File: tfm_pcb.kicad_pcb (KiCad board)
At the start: 2 copper layers, 73 x 55 mm, 70 parts, among them J1 Conn_01x02_MountingPin, J12 Conn_01x01_Pin, J13 Conn_01x01_Pin, J15 Conn_01x01_Socket, J16 Conn_01x01_Socket, J17 Conn_01x01_Socket, J18 Conn_01x01_Socket, J19 Conn_01x01_Socket, J2 USB_B_Micro, J20 Conn_01x01_Socket, J21 Conn_01x01_Socket, J22 Conn_01x01_Socket, J23 Conn_01x01_Socket, J24 Conn_01x01_Socket, J3 Mounting Pin, J5 Conn_01x01_Pin, J6 Conn_01x01_Pin, U1 ESP32-S3-WROOM-2, U2 MCP73871-2CC, U3 ADS1292IPBS, U4 LSM6DS3, U5 USBLC6-2SC6, U6 XC6220B331MR, U7 USBLC6-2SC6

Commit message: Separar DVDD de la ferrita, filtro amortiguado en AVDD y conector THT de electrodos
- DVDD del ADS1292 (y C6/C7) a +3.3V sin ferrita.
- Rama analógica: FB1 + R15 (2.2 ohm) + C26 (10 uF) antes de AVDD; filtro
  colocado junto al AFE manteniendo el puente en B.Cu bajo el ADS1292.
- C12 (VREFP) sincronizado a 10 uF en la PCB.
- Esquemático: pastillas de electrodos sustituidas por conector THT 1x10.
- Documentación movida a docs_local/ (ignorada por git).

Co-Authored-By: Claude Opus 5.5 <noreply@anthropic.com>
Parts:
- added C26: 10u, Capacitor_SMD:C_0805_2012Metric, F.Cu at (168.4, 78.5)
- added R15: 2.2, Resistor_SMD:R_0603_1608Metric, F.Cu at (165.8, 77.5)
- C12: value 1u -> 10u
- FB1: value (none) -> FerriteBead
- moved FB1 25.1 mm to (162.6, 77.5)
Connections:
- C6 pad 2: +3.3VA -> +3.3V
- C7 pad 2: +3.3VA -> +3.3V
- FB1 pad 2: +3.3VA -> Net-(FB1-Pad2)
- U3 pad 23: +3.3VA -> +3.3V
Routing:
- net +3.3V: track 87.0 -> 126.3 mm, vias 2 -> 4
- net +3.3VA: track 49.6 -> 19.7 mm, vias 2 -> 0
- net Net-(FB1-Pad2): track 0.00 -> 1.59 mm

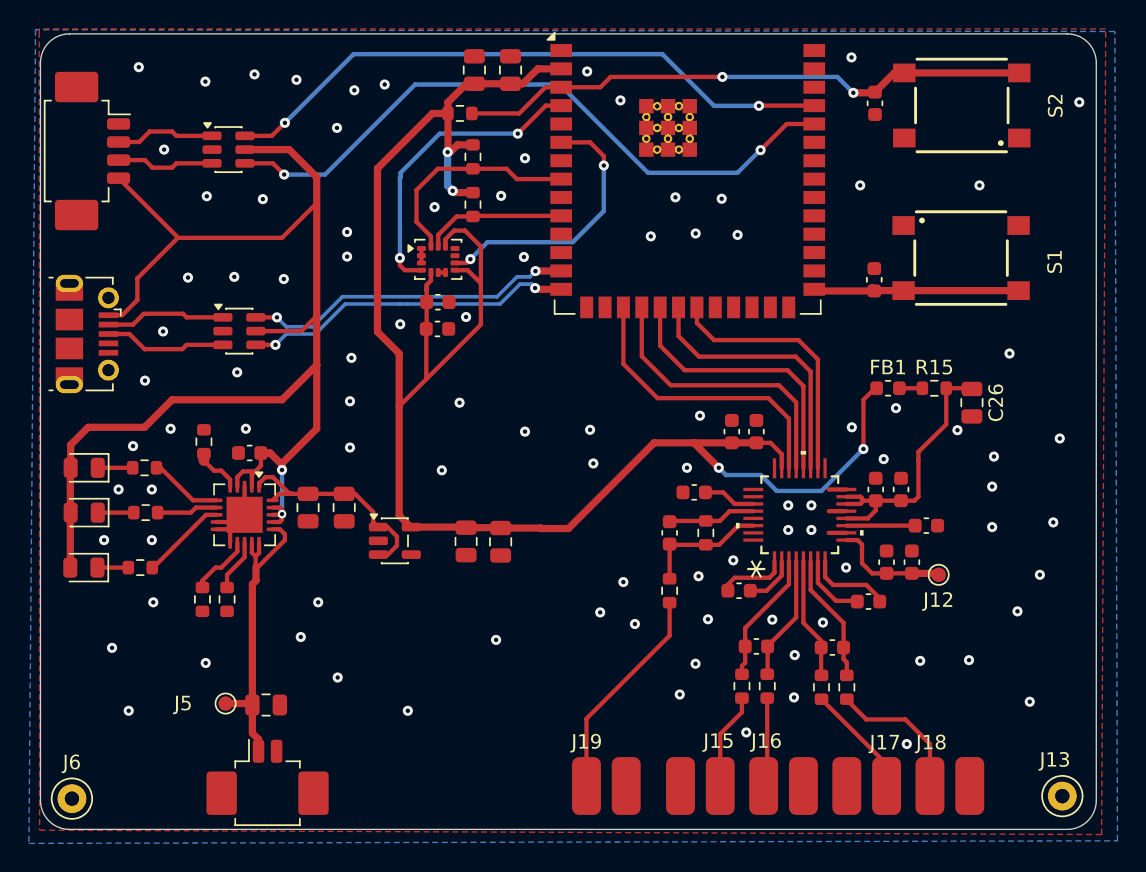
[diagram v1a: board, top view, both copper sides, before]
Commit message: Conector J4 THT reordenado, selector de malla JP1 y net SHIELD
- J4 (tira 1x10): 1 RLD, 2-3 malla, 4 IN1N, 5 IN1P, 6-7 malla, 8 IN2N,
  9 IN2P, 10 malla; etiquetas EL1N/EL1P/EL2N/EL2P en lugar del abanico.
- Net SHIELD con las cinco mallas; JP1 (tira 3 pines): 1-2 INRLD (T2),
  2-3 GND (T1). Serigrafía de función en J4 y JP1.
- Ajustes de layout del autor: filtro FB1/R15/C26 junto a C9, C26 en
  0603, SHIELD por B.Cu en el borde, rutado de EL2P.

Co-Authored-By: Claude Opus 5.5 <noreply@anthropic.com>
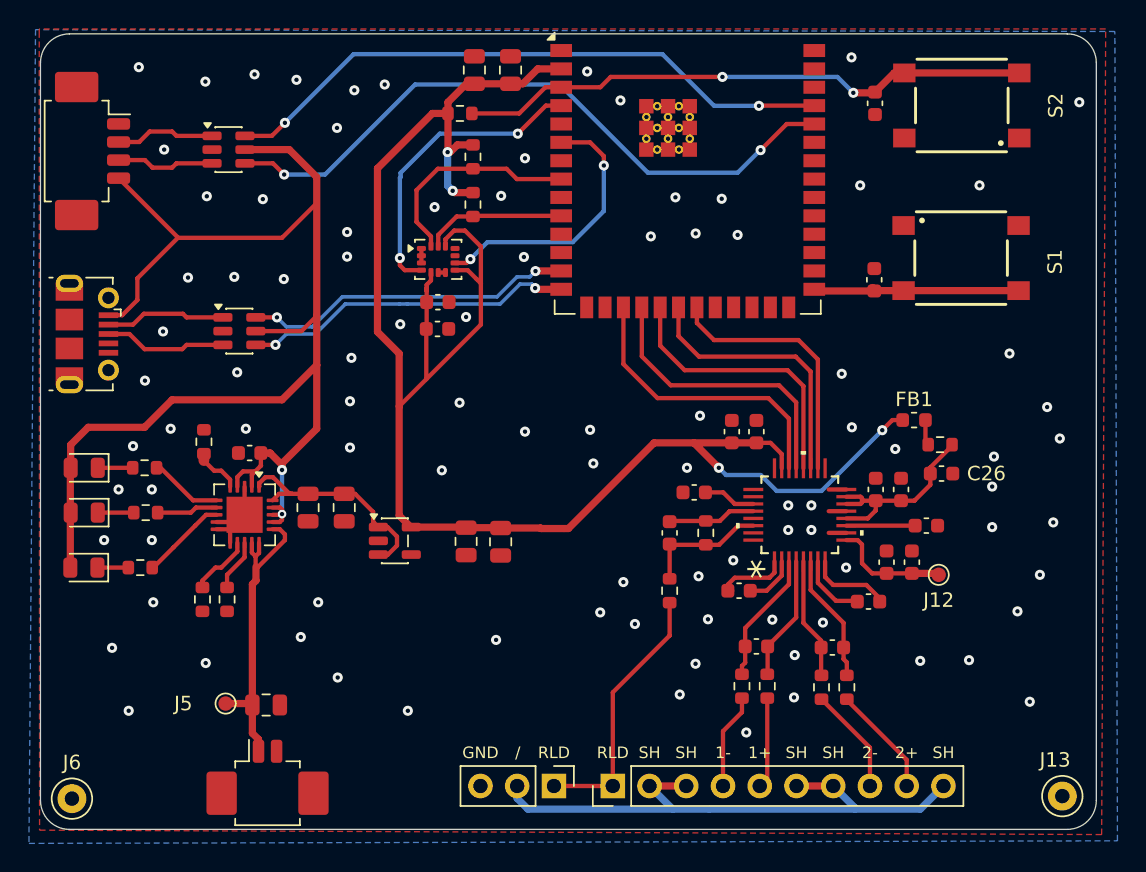
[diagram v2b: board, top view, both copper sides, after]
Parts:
- removed J15, J16, J17, J18, J19, J20, J21, J22, J23, J24: Conn_01x01_Socket, Connector_Wire:SolderWirePad_1x01_SMD_2x4mm
- added J4: Conn_01x10_Pin, Connector_PinHeader_2.54mm:PinHeader_1x10_P2.54mm_Vertical, F.Cu at (143.6, 105.0)
- added JP1: SHIELD_SEL, Connector_PinHeader_2.54mm:PinHeader_1x03_P2.54mm_Vertical, F.Cu at (139.5, 105.0)
- C26: footprint Capacitor_SMD:C_0805_2012Metric -> Capacitor_SMD:C_0603_1608Metric
- moved C26 5.33 mm to (166.3, 83.4), turned to 0 degrees
- moved R15 3.92 mm to (166.2, 81.4)
- moved FB1 2.84 mm to (164.4, 79.7)
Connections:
- R10 pad 1: Net-(J18-Pin_1) -> /EL2P
- R7 pad 1: Net-(J15-Pin_1) -> /EL1N
- R8 pad 1: Net-(J16-Pin_1) -> /EL1P
- R9 pad 1: Net-(J17-Pin_1) -> /EL2N
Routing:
- net /SHIELD: track 0.00 -> 40.9 mm
- net Net-(J18-Pin_1): track 9.96 -> 0.00 mm
- net Net-(J17-Pin_1): track 7.86 -> 0.00 mm
- net /EL2P: track 0.00 -> 7.71 mm
- net /EL2N: track 0.00 -> 7.39 mm
- net Net-(J15-Pin_1): track 6.70 -> 0.00 mm
- net /EL1N: track 0.00 -> 6.62 mm
- net /EL1P: track 0.00 -> 6.30 mm
- net Net-(J16-Pin_1): track 6.18 -> 0.00 mm
- net +3.3VA: track 19.7 -> 14.1 mm
- net /INRLD: track 15.1 -> 18.4 mm
- net +3.3V: track 126.3 -> 125.2 mm
- net GND: vias 95 -> 94
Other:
- board text added: "/"
- board text added: "1+"
- board text added: "1-"
- board text added: "2+"
- board text added: "2-"
- board text added: "GND"
- board text added: "RLD"
- board text added: "SH"

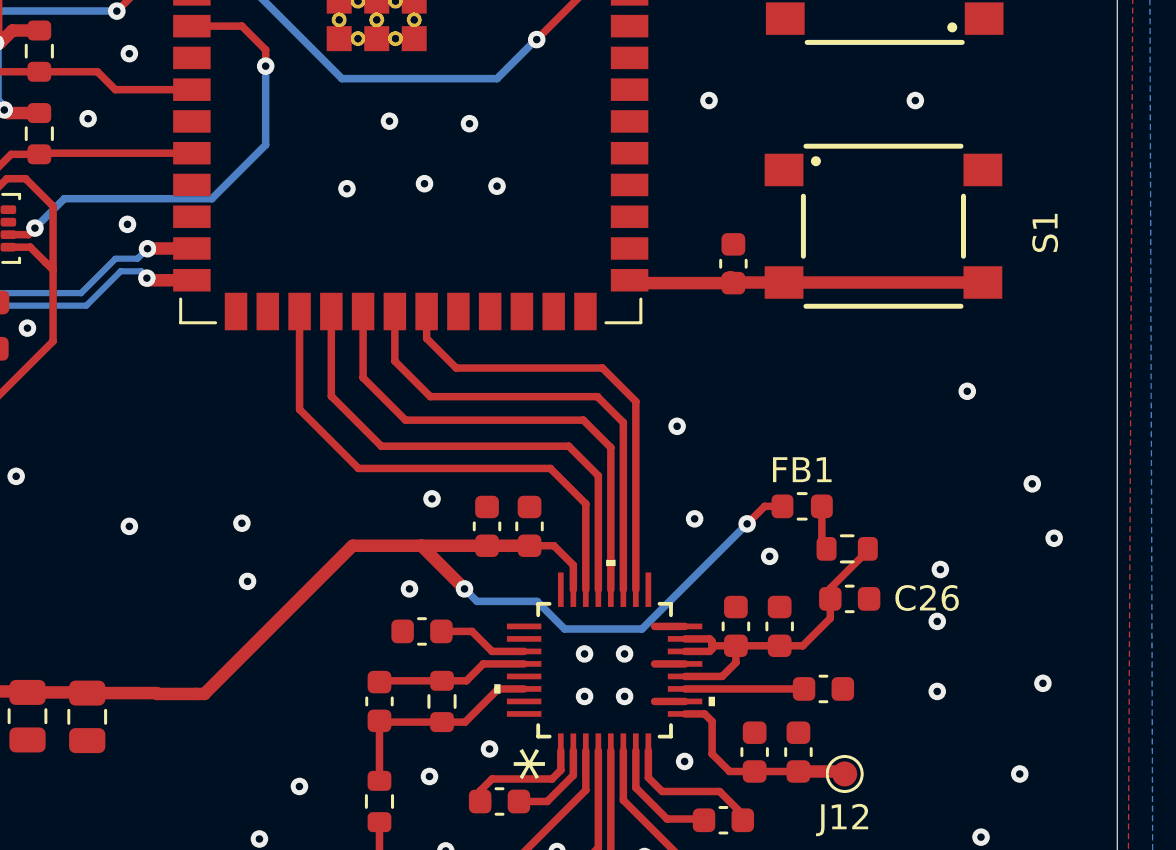
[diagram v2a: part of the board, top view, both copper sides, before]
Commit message: PWDN del ADS1292 controlado por IO38 y reordenado del desacoplo de AVDD
- PWDN/RESET (U3.15) separado de +3.3VA y llevado a IO38 (U1.31) con
  pull-down R16 = 10 kOhm; rutado por la derecha del bus SPI con salto
  en B.Cu bajo la pista de BOOT.
- CLKSEL (U3.14) sigue en +3.3VA.
- Ajustes de layout del autor: cadena AVDD R15 -> C26 -> C9 -> C8 -> pin,
  vías de GND junto a los condensadores, vías de cosido recolocadas y
  START (U3.16) unido al plano por el relleno de cobre.

Co-Authored-By: Claude Opus 5.5 <noreply@anthropic.com>
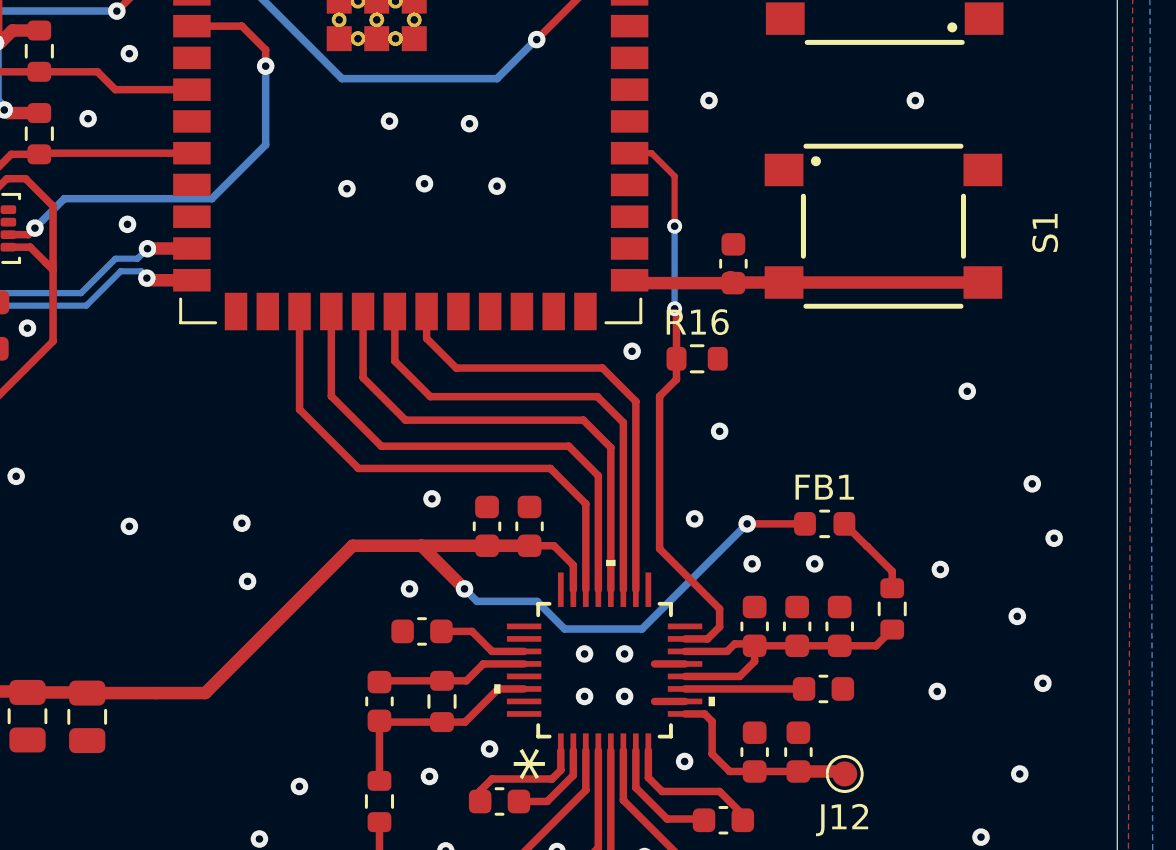
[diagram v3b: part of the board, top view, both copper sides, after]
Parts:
- added R16: 10k, Resistor_SMD:R_0603_1608Metric, F.Cu at (160.2, 73.8)
- moved R15 3.00 mm to (168.0, 83.8), turned to -90 degrees
- moved C26 1.17 mm to (165.9, 84.5), turned to 90 degrees
- moved FB1 1.14 mm to (165.3, 80.4)
- moved C8 0.75 mm to (162.5, 84.5)
- moved C9 0.70 mm to (164.2, 84.5)
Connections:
- U1 pad 31: unconnected-(U1-IO38-Pad31) -> /ADS_PWDN
- U3 pad 15: +3.3VA -> /ADS_PWDN
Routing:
- net /ADS_PWDN: track 0.00 -> 23.1 mm, vias 0 -> 2
- net Net-(FB1-Pad2): track 1.78 -> 3.37 mm
- net +3.3VA: track 14.1 -> 12.5 mm
- net GND: track 12.5 -> 11.3 mm, vias 94 -> 96
- net +3.3V: track 125.2 -> 125.8 mm

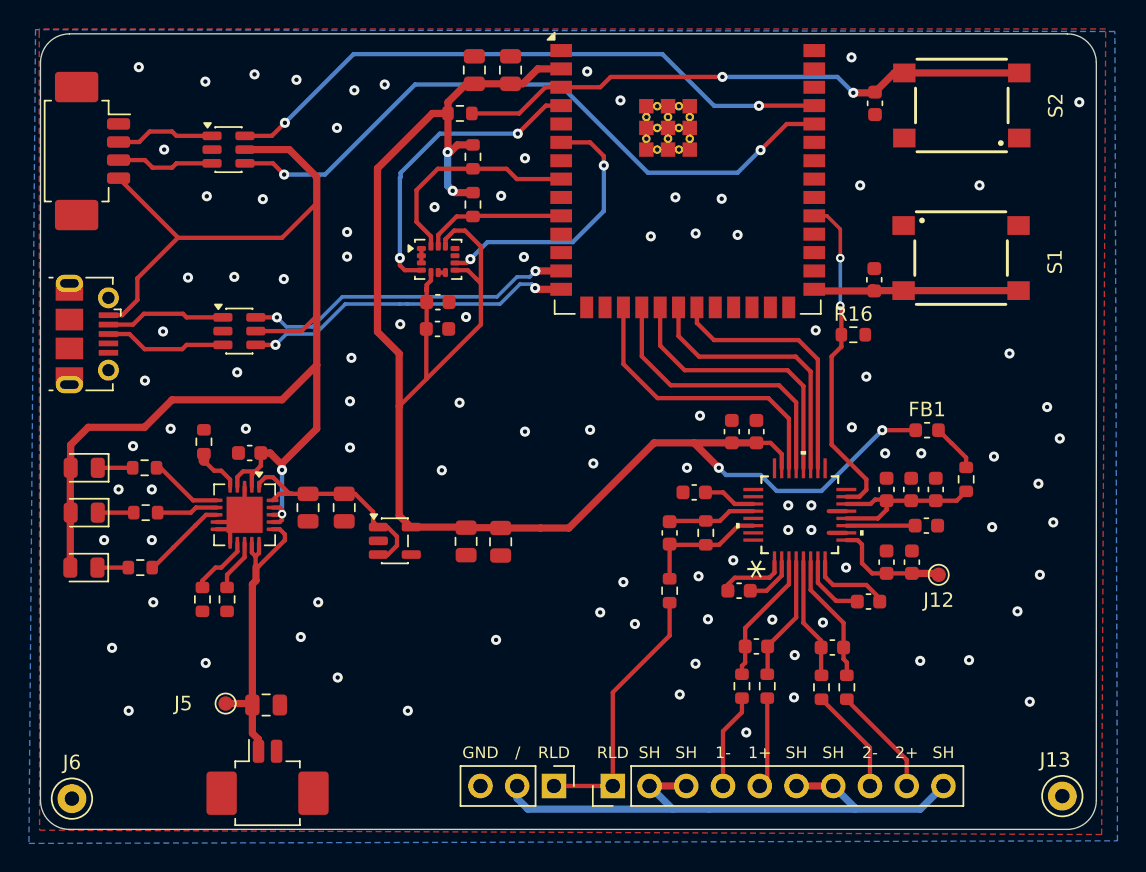
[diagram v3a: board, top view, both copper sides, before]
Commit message: Arreglos previos a fabricación: pines sin usar del ADS1292, EN, C2, vías térmicas y masas
- ADS1292: IN3P/IN3N/RLDIN a AVDD (pista bajo el encapsulado desde el pin 12);
  GPIO1/GPIO2 a DGND con R19/R18 de 10 kOhm.
- ESP32 EN: R1 = 10 kOhm, C1 = 1 uF a 4.5 mm del pin.
- MCP73871: C2 = 10 uF en 0805; huella con 4 vías térmicas de 0.3 mm.
- U4: vías de GND para sus pads de masa; conexión sólida al plano en
  U5/U6/U7/J2/R18/R19. DRC sin errores.

Co-Authored-By: Claude Opus 5.5 <noreply@anthropic.com>
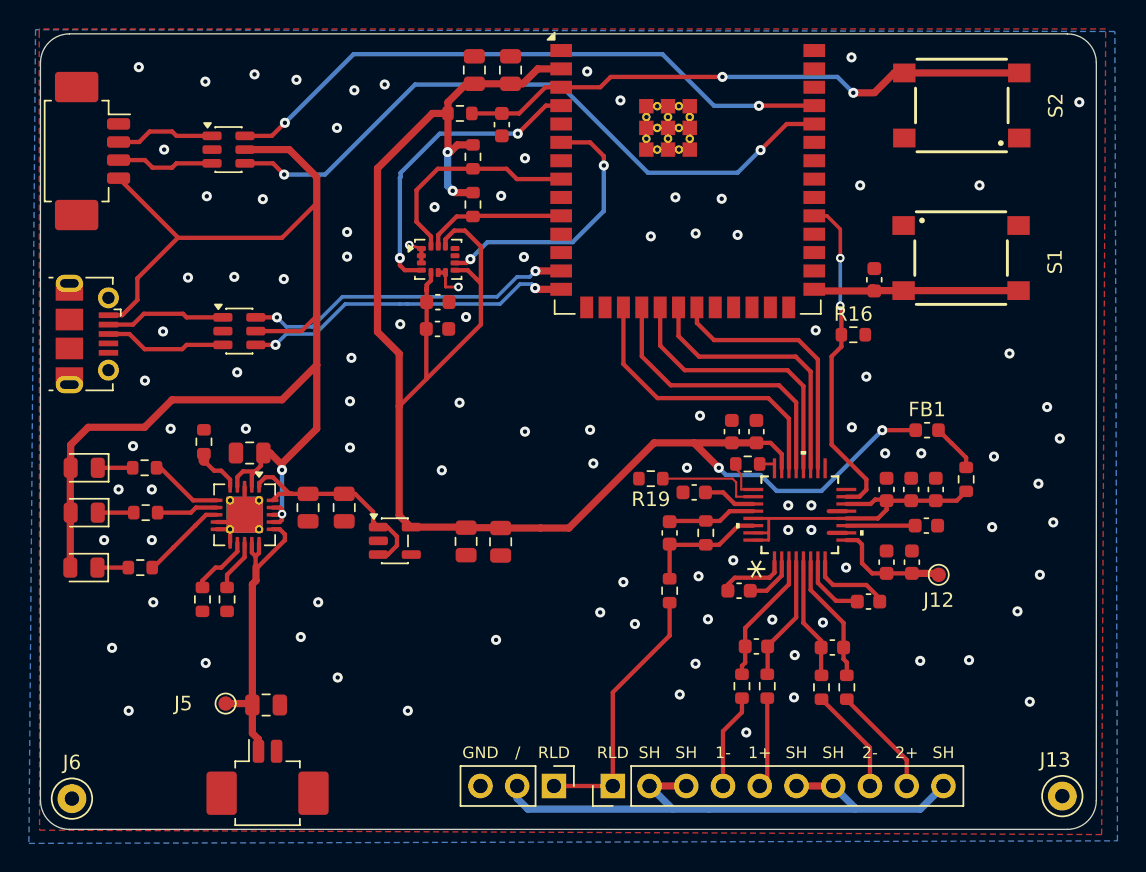
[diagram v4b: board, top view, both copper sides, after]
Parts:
- added R18: 10k, Resistor_SMD:R_0603_1608Metric, F.Cu at (152.9, 82.7)
- added R19: 10k, Resistor_SMD:R_0603_1608Metric, F.Cu at (146.2, 83.8)
- C1: value 1nF -> 1u
- C2: value C -> 10u; footprint Capacitor_SMD:C_0603_1608Metric -> Capacitor_SMD:C_0805_2012Metric
- R1: value R -> 10k
- U2: footprint Package_DFN_QFN:QFN-20-1EP_4x4mm_P0.5mm_EP2.5x2.5mm -> Package_DFN_QFN:QFN-20-1EP_4x4mm_P0.5mm_EP2.5x2.5mm_ThermalVias
- moved C1 25.8 mm to (135.9, 59.3)
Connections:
- U3 pad 25: unconnected-(U3-GPIO2/RCLK2-Pad25) -> Net-(U3-GPIO2/RCLK2)
- U3 pad 26: unconnected-(U3-GPIO1/RCLK1-Pad26) -> Net-(U3-GPIO1/RCLK1)
- U3 pad 29: unconnected-(U3-RLDIN/RLDREF-Pad29) -> +3.3VA
- U3 pad 31: unconnected-(U3-RESP_MODP/IN3P-Pad31) -> +3.3VA
- U3 pad 32: unconnected-(U3-RESP_MODN/IN3N-Pad32) -> +3.3VA
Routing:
- net +3.3VA: track 12.5 -> 22.6 mm
- net Net-(U3-GPIO1/RCLK1): track 0.00 -> 7.36 mm
- net GND: track 11.3 -> 15.1 mm, vias 96 -> 98
- net Net-(U3-GPIO2/RCLK2): track 0.00 -> 2.37 mm

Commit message: Reorganización de layout del autor: zona ADS1292, SPI, acelerómetro y +3.3V
- Recolocación de la zona del ADS1292 (C8, C9, C10, C11, C18, C26, R11,
  R12, R15, R18, R19) y nuevo rutado de SPI a 0.25 mm.
- Acelerómetro U4 recolocado, con vía de GND central e INT1 por F.Cu.
- Tronco de +3.3V y alimentación del filtro de AVDD rehechos.
- C8 a 0402 en el esquemático; ancho de pista 0.25 mm añadido al proyecto.

Pendiente: C11 en 0402 en la PCB y 0603 en el esquemático (paridad),
alivio térmico del pad 7 de U4 y dos pistas colgando (+5V, +3.3V).

Co-Authored-By: Claude Opus 5.5 <noreply@anthropic.com>
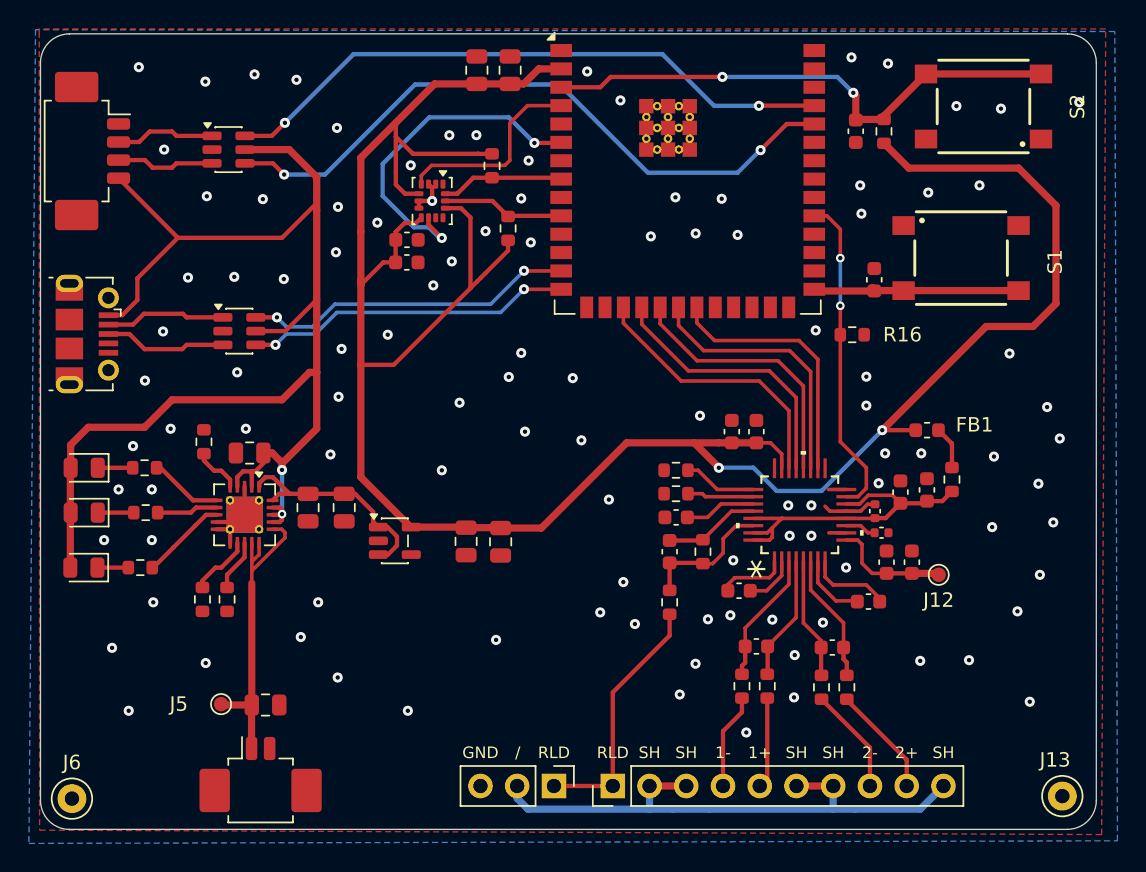
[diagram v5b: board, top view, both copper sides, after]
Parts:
- C11, C8: footprint Capacitor_SMD:C_0603_1608Metric -> Capacitor_SMD:C_0402_1005Metric
- moved R1 29.3 mm to (162.3, 59.7), turned to 90 degrees
- moved C1 24.5 mm to (160.4, 59.7)
- moved C19 5.07 mm to (129.3, 68.8)
- moved R18 4.98 mm to (147.9, 83.2), turned to 180 degrees
- moved C20 4.81 mm to (129.3, 67.2)
- moved U4 4.06 mm to (131.1, 64.5), turned to -90 degrees
- moved C11 3.14 mm to (162.2, 87.5)
- moved R13 2.94 mm to (136.3, 66.5), turned to 90 degrees
- moved C10 2.13 mm to (147.9, 86.4)
- moved R19 2.03 mm to (147.9, 84.8)
- moved C8 1.70 mm to (161.7, 86.0)
- moved S2 1.50 mm to (169.2, 58.0)
- moved R14 1.46 mm to (135.2, 62.1)
- moved R11 1.32 mm to (149.8, 88.8)
- moved C18 1.30 mm to (147.5, 88.8)
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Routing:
- net +3.3V: track 125.8 -> 169.4 mm, vias 4 -> 2
- net /INT1: track 21.1 -> 13.8 mm, vias 2 -> 0
- net /SDA: track 15.2 -> 8.50 mm
- net /INT2: track 19.0 -> 23.7 mm
- net Net-(U3-GPIO2/RCLK2): track 2.37 -> 5.65 mm
- net Net-(U1-EN): track 40.0 -> 37.2 mm
- net Net-(U3-GPIO1/RCLK1): track 7.36 -> 4.61 mm
- net Net-(U3-VCAP1): track 4.76 -> 2.16 mm
- net /DRDY: track 20.4 -> 19.0 mm
- net /SCL: track 9.82 -> 8.51 mm
- net Net-(U3-VCAP2): track 3.64 -> 4.94 mm
- net /SHIELD: track 40.9 -> 39.6 mm
- net GND: track 15.1 -> 16.3 mm, vias 98 -> 108
- net /MISO: track 19.9 -> 18.8 mm
- net /SCK: track 19.4 -> 18.5 mm
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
